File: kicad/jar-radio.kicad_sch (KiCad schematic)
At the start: 55 parts, among them J1 USB-C 5V, J2 BATT (PH), J3 ANT (XH), Q1 AO3401A, U1 Si4825-A10, U2 NS8002, U3 TP4056, U4 XC6206P332MR, U5 XC61CN2702MR, Y1 32.768kHz

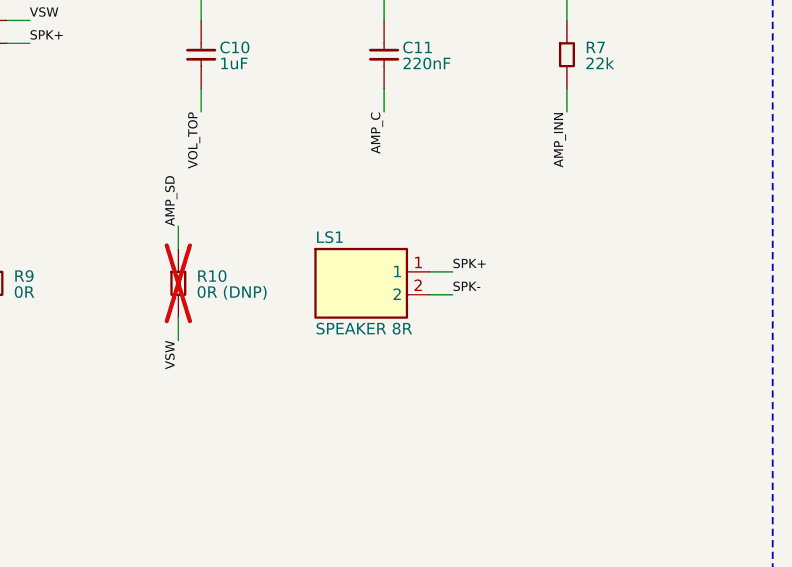
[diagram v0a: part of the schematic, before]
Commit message: Speaker on PH socket, USB-C placed by JLC (two-sided), BOM/cost model/plan builder updates
Co-Authored-By: Claude Opus 5.5 <noreply@anthropic.com>
Claude-Session: https://claude.ai/code/session_01UChZ4MGw6SzykNSB399iC4
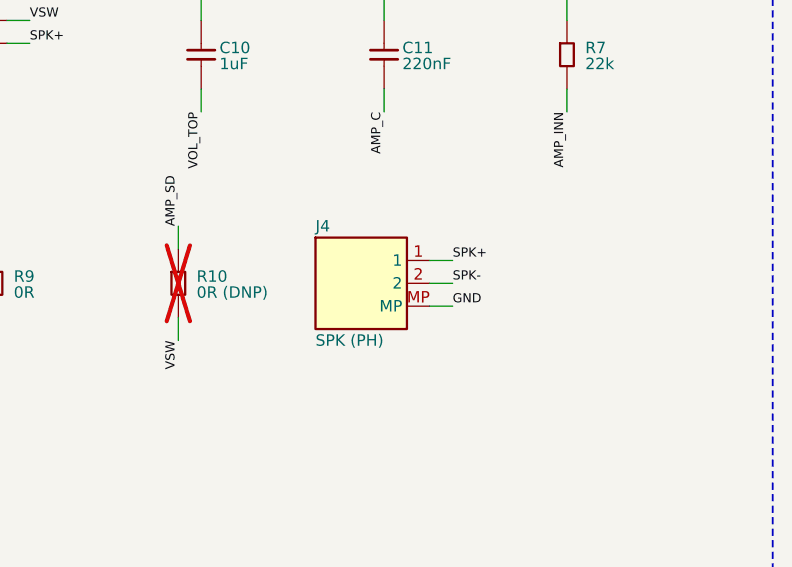
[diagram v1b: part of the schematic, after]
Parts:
- removed LS1: SPEAKER 8R, jar-radio:Speaker_Wire_Pads_P5, symbol jar-radio:Conn_2
- added J4: SPK (PH), Connector_JST:JST_PH_B2B-PH-SM4-TB_1x02-1MP_P2.00mm_Vertical, symbol jar-radio:Conn_2_MP
- J1: Assembly Hand -> (none)
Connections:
- net GND: now also J4.MP
- net SPK+: now also J4.1
- net SPK-: now also J4.2

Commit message: Rev F.2: Alps 20k switched pot, amp gain for 20k pot, 22uF/0603 LED swaps, XC61C pinout fix, JLC quote files
Co-Authored-By: Claude Opus 5.5 <noreply@anthropic.com>
Claude-Session: https://claude.ai/code/session_01UChZ4MGw6SzykNSB399iC4
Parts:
- added C21: 22uF, Capacitor_SMD:C_0805_2012Metric, symbol jar-radio:C
- C11: value 220nF -> 100nF; LCSC C307462 -> C14663; MPN CL10A224KB8NNNC -> CC0603KRX7R9BB104
- C18, C7: value 47uF -> 22uF; LCSC C16780 -> C45783; MPN CL21A476MQYNNNE -> CL21A226MAQNNNE
- C3: LCSC (none) -> C19666
- D2: footprint LED_SMD:LED_1206_3216Metric_ReverseMount_Hole1.8x2.4mm -> LED_SMD:LED_0603_1608Metric; LCSC C2892757 -> C2286; MPN 24-21SURC/S530-A3/TR8 -> KT-0603R
- D3: footprint LED_SMD:LED_1206_3216Metric_ReverseMount_Hole1.8x2.4mm -> LED_SMD:LED_0603_1608Metric; LCSC C4749157 -> C72043; MPN 25-21/GHC-YSU/2A -> 19-217/GHC-YR1S2/3T
- D4: LCSC (none) -> C5139344; MPN PESD5V0F1BL (TBD) -> PESD5V0F1BL
- J2: footprint Connector_JST:JST_PH_B2B-PH-SM4-TB_1x02-1MP_P2.00mm_Vertical -> Connector_JST:JST_PH_S2B-PH-SM4-TB_1x02-1MP_P2.00mm_Horizontal; LCSC (none) -> C295747; MPN B2B-PH-SM4-TB(LF)(SN) -> S2B-PH-SM4-TB(LF)(SN)
- J4: value SPK (PH) -> SPK (XH); footprint Connector_JST:JST_PH_B2B-PH-SM4-TB_1x02-1MP_P2.00mm_Vertical -> jar-radio:Connector_XH-SMD_GSwitch_GT-A2501WRS-102_1x02_P2.50mm_Horizontal; LCSC (none) -> C23067528; MPN B2B-PH-SM4-TB(LF)(SN) -> GT-A2501WRS-102SBT01
- L1: LCSC (none) -> C98080
- R4: LCSC (none) -> C22775
- R7: value 22k -> 47k; LCSC C31850 -> (none); MPN 0603WAF2202T5E -> 0603WAF4702T5E
- R8: value 220k -> 560k; LCSC C22961 -> (none); MPN 0603WAF2203T5E -> 0603WAF5603T5E
- RV1: value B50K + SW -> 20k + SW; Assembly Hand -> (none); LCSC (none) -> C470569; MPN RV097NS B50K -> RK0971111Z0P
- U5: LCSC (none) -> C112139; MPN XC61CN2702MR -> XC61CN2702MR-G
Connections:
- net +3V3: now also U5.3 (VIN); no longer U5.2 (VIN)
- net GND: now also U5.2 (VSS), C21.2; no longer U5.3 (VSS)
- net TUNE1: now also C21.1

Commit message: Apply JLC BOM-tool findings: Basic swaps for C9, band ladder, R8; record results
Co-Authored-By: Claude Opus 5.5 <noreply@anthropic.com>
Claude-Session: https://claude.ai/code/session_01UChZ4MGw6SzykNSB399iC4
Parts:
- added R17: 100k, Resistor_SMD:R_0603_1608Metric, symbol jar-radio:R
- C9: value 1nF C0G -> 1nF; LCSC C163508 -> C1588; MPN CL10C102JB8NNNC -> CL10B102KB8NNNC
- R5: value 430k -> 330k; LCSC C25969 -> C23137; MPN 0603WAF4303T5E -> 0603WAF3303T5E
- R7: LCSC (none) -> C25819
- R8: value 560k -> 470k; LCSC (none) -> C23178; MPN 0603WAF5603T5E -> 0603WAF4703T5E
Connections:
- net BAND: now also R17.2; no longer R5.2
- new net BAND_M: R17.1, R5.2

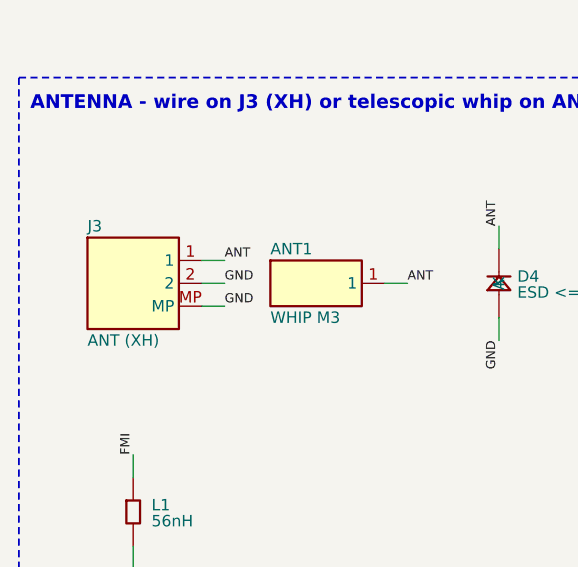
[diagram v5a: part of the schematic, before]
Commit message: Rev F.3: antenna solder hole, pot is horizontal (not usable), battery protection plan, alternatives search list
Co-Authored-By: Claude Opus 5.5 <noreply@anthropic.com>
Claude-Session: https://claude.ai/code/session_01UChZ4MGw6SzykNSB399iC4
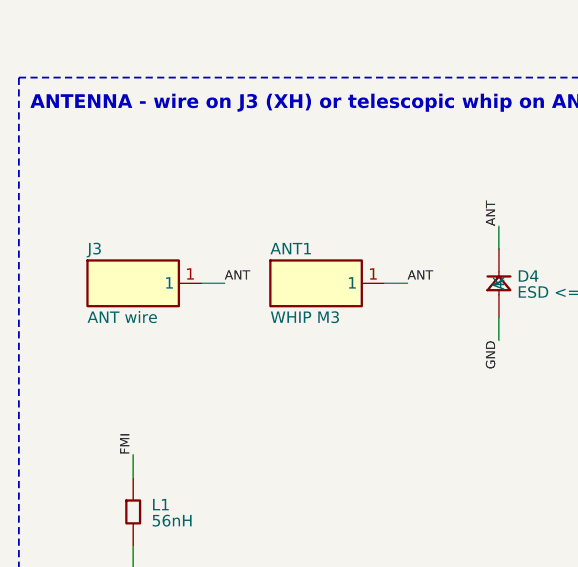
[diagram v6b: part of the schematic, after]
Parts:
- removed J3: ANT (XH), jar-radio:Connector_XH-SMD_GSwitch_GT-A2501WRS-102_1x02_P2.50mm_Horizontal, symbol jar-radio:Conn_2_MP
- added J3: ANT wire, jar-radio:Antenna_Wire_Solder_D1.0, symbol jar-radio:Conn_1
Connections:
- net ANT: now also J3.1

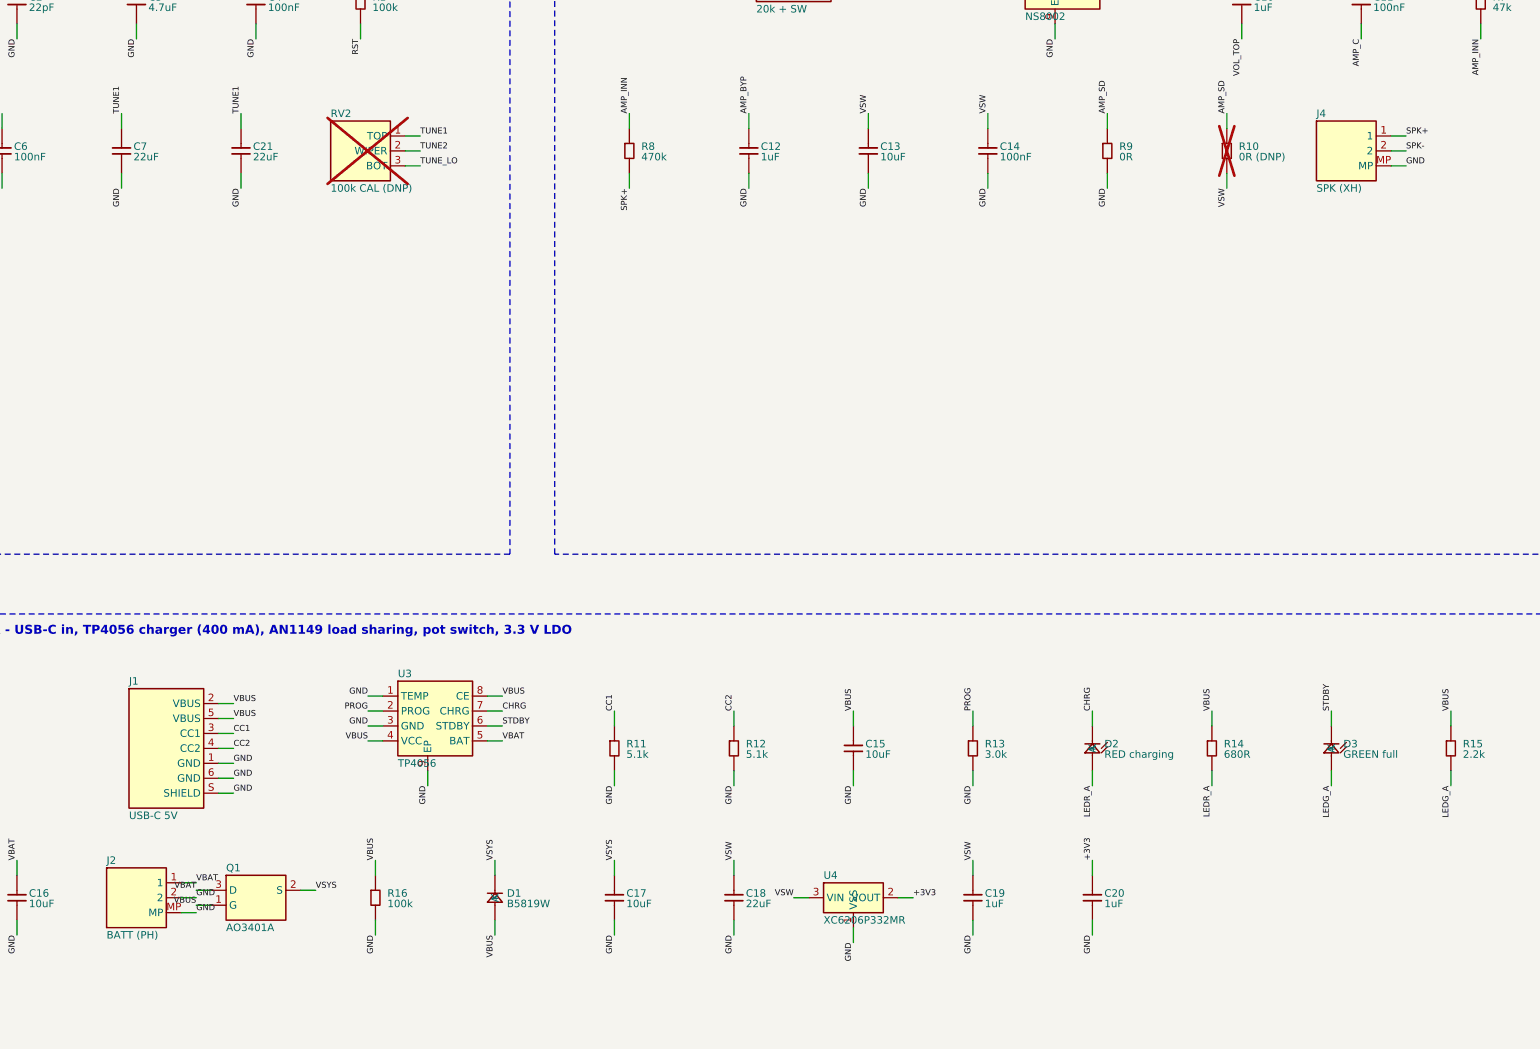
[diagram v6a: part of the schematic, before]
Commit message: Rev F.6: speaker datasheet review, 18650 holder tab-slot footprint, protection IC comparison
Co-Authored-By: Claude Opus 5.5 <noreply@anthropic.com>
Claude-Session: https://claude.ai/code/session_01UChZ4MGw6SzykNSB399iC4
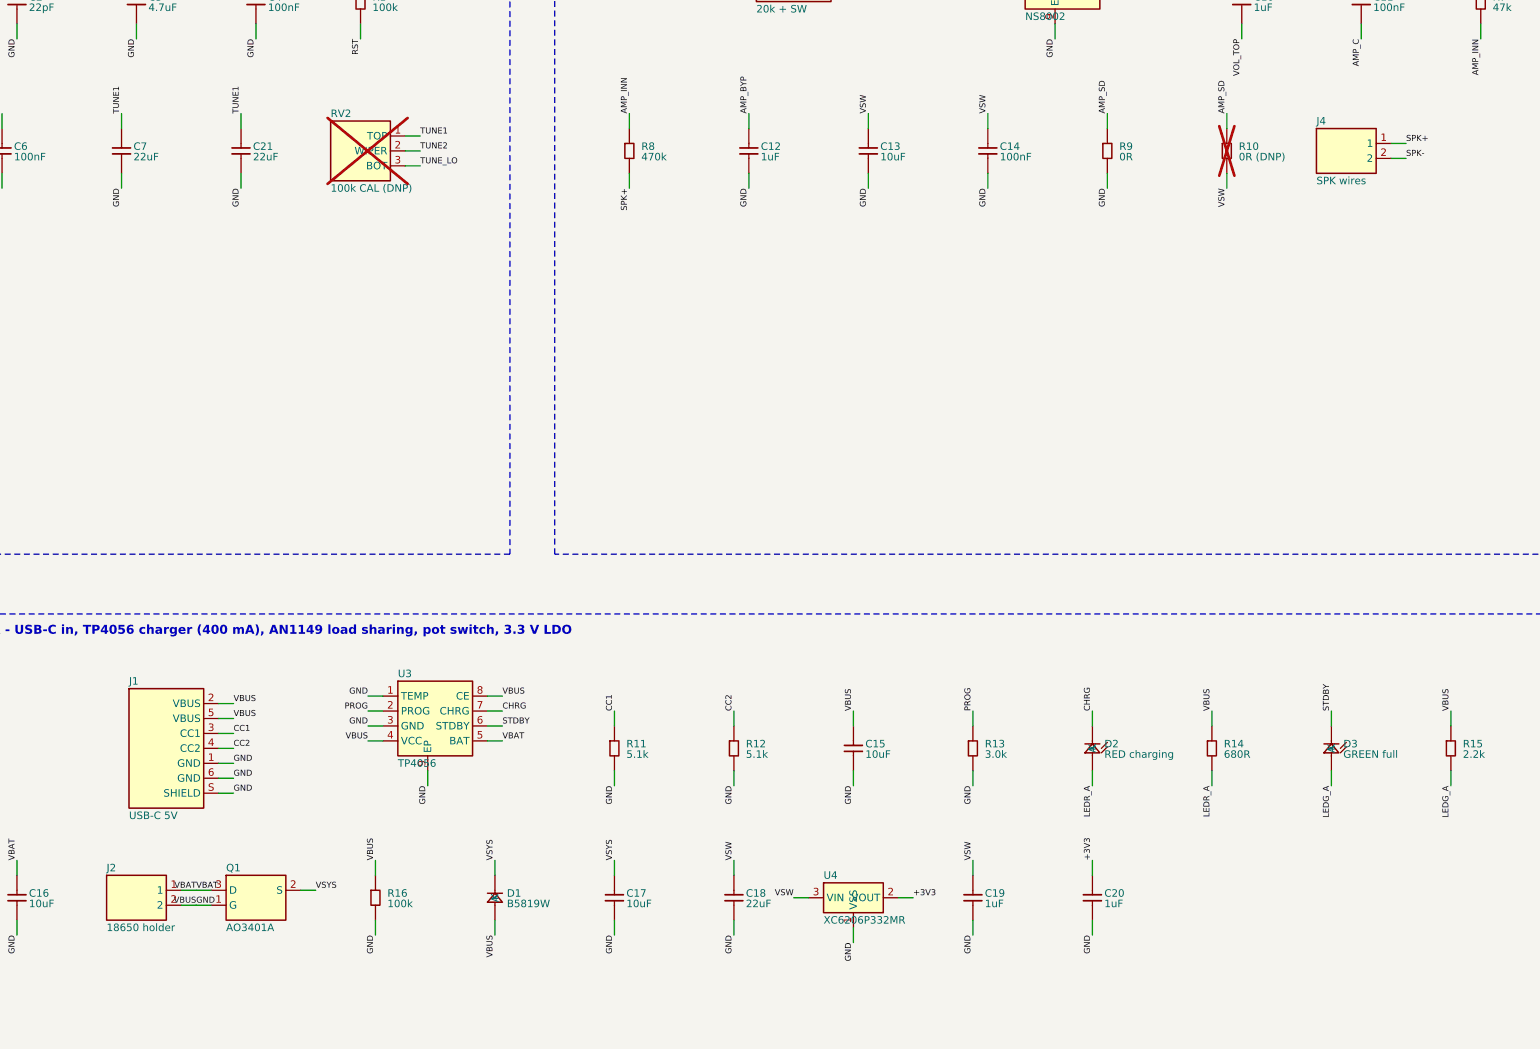
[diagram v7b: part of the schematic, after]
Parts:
- removed J2: BATT (PH), Connector_JST:JST_PH_S2B-PH-SM4-TB_1x02-1MP_P2.00mm_Horizontal, symbol jar-radio:Conn_2_MP
- removed J4: SPK (XH), jar-radio:Connector_XH-SMD_GSwitch_GT-A2501WRS-102_1x02_P2.50mm_Horizontal, symbol jar-radio:Conn_2_MP
- added J2: 18650 holder, jar-radio:Battery_Holder_Tab_Slot_Plus_Wire, symbol jar-radio:Conn_2
- added J4: SPK wires, jar-radio:Speaker_Wire_Pads_P5, symbol jar-radio:Conn_2
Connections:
- net VBUS is gone; now on net GND: C15.1, D1.2 (A), J1.2 (VBUS), J1.5 (VBUS), Q1.1 (G), R14.1, R15.1, R16.1, U3.4 (VCC), U3.8 (CE)
- net GND: now also J2.2
- net SPK+: now also J4.1
- net SPK-: now also J4.2
- net VBAT: now also J2.1

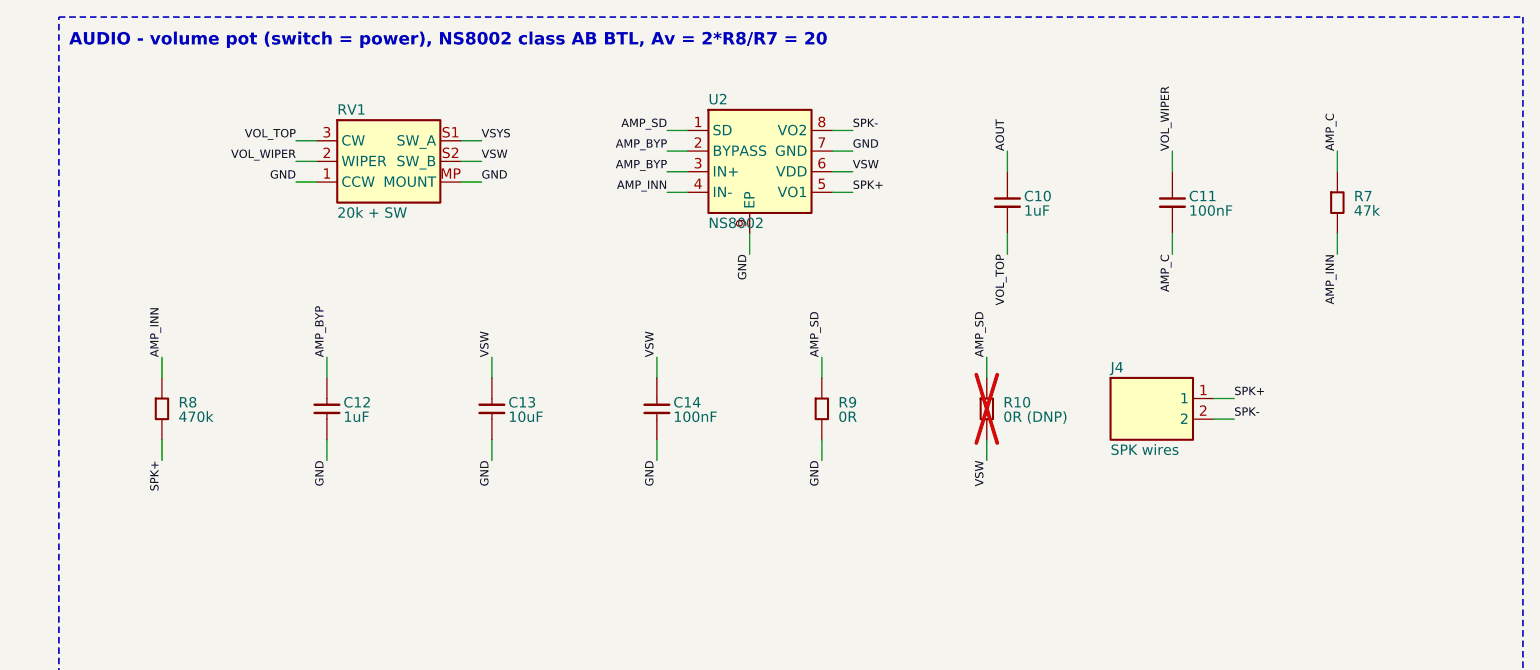
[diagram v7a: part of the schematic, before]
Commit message: Rev F.7: PTV09A-4 rear-mount pot + slide power switch, 18650 holder slot from drawing, antenna tie holes, XB8089D chosen
Co-Authored-By: Claude Opus 5.5 <noreply@anthropic.com>
Claude-Session: https://claude.ai/code/session_01UChZ4MGw6SzykNSB399iC4
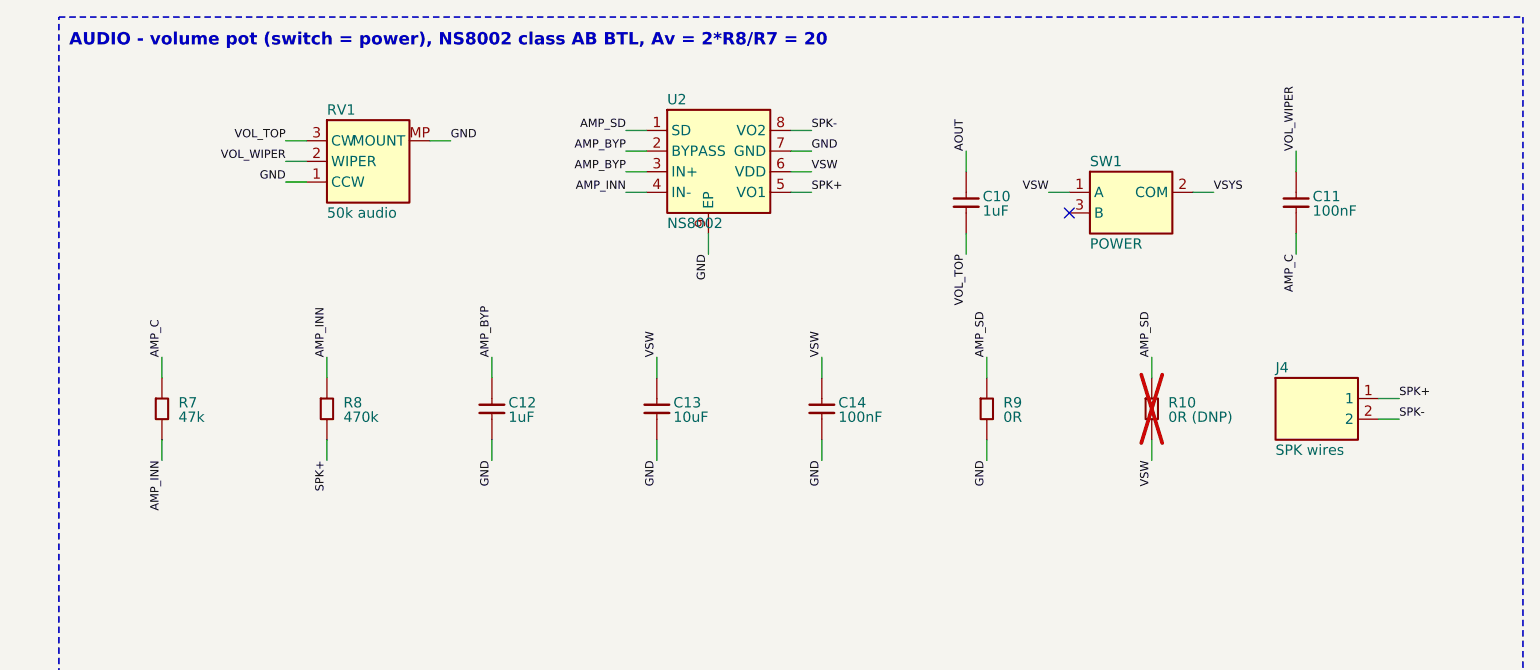
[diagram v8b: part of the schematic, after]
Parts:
- removed RV1: 20k + SW, jar-radio:Potentiometer_RV097NS_Switch_Vertical_PROVISIONAL, symbol jar-radio:Pot_Switch
- added RV1: 50k audio, jar-radio:Potentiometer_Bourns_PTV09A-4_RearMount, symbol jar-radio:Pot3
- added SW1: POWER, Button_Switch_SMD:SW_SPDT_PCM12, symbol jar-radio:SW_SPDT
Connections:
- net GND: now also RV1.1 (CCW), RV1.MP (MOUNT)
- net VOL_TOP: now also RV1.3 (CW)
- net VOL_WIPER: now also RV1.2 (WIPER)
- net VSW: now also SW1.1 (A)
- net VSYS: now also SW1.2 (COM)
- no-connect marks 2 -> 3
